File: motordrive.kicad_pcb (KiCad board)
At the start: 2 copper layers, 160 x 111.4 mm, 32 parts, among them K1 CONN_3, M1 ARDUINO, P2 CONN_25, U1 5VSWREG, U2 74HC595, U3 74HC595, U4 LM2903, U5 ULN2803, U6 ULN2803

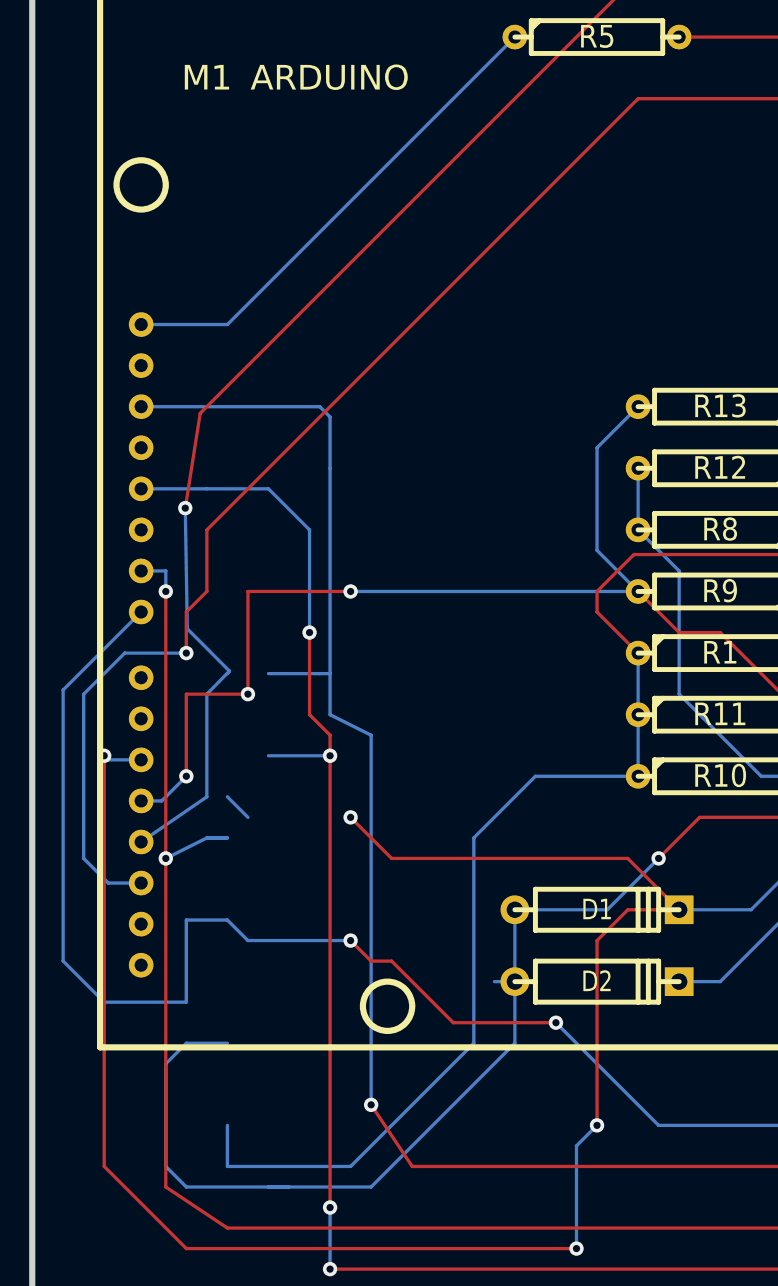
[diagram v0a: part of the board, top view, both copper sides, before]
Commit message: Tidied .brd and saved, no other changes
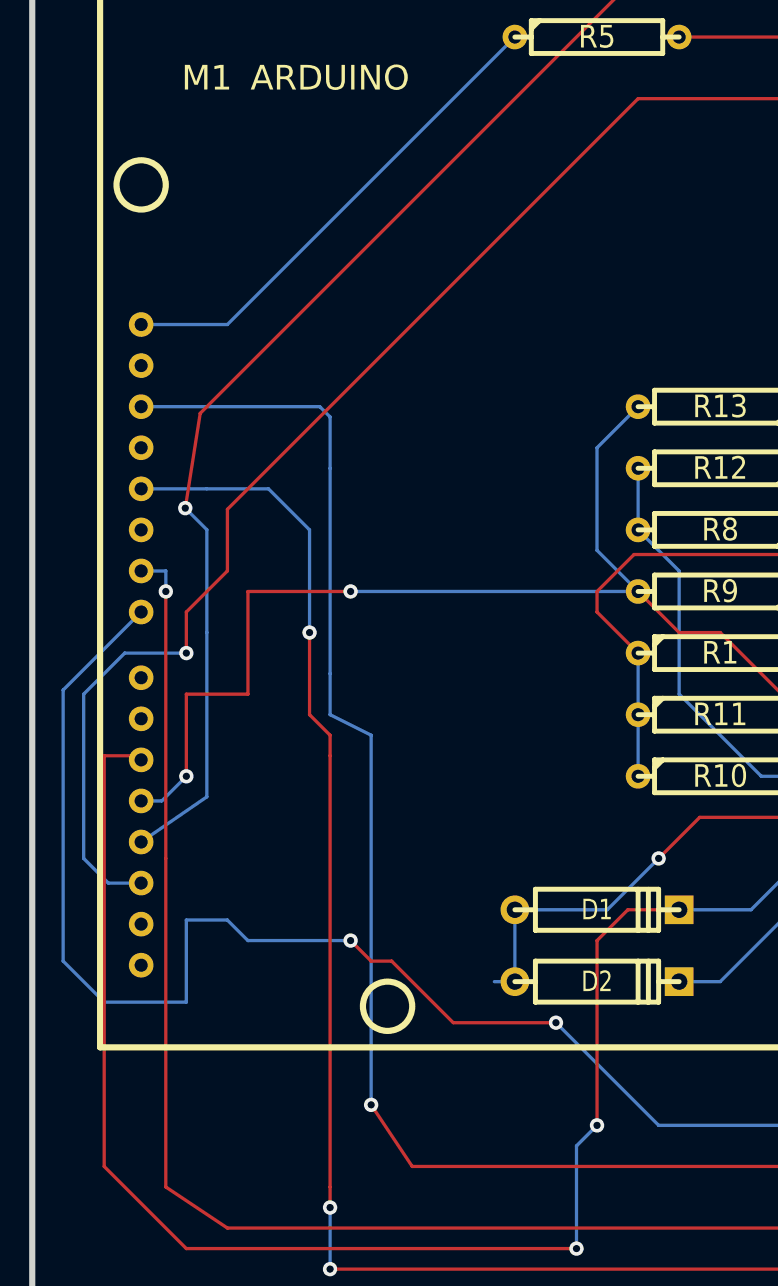
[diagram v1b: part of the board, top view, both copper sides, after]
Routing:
- net +5V: track 253.0 -> 207.6 mm
- net GND: track 302.6 -> 261.0 mm
- net N-0000037: track 147.8 -> 123.3 mm, vias 4 -> 2
- net N-0000018: track 167.7 -> 162.3 mm, vias 3 -> 2
- net N-0000049: track 150.6 -> 146.8 mm, vias 4 -> 3
- net N-0000023: track 184.2 -> 180.4 mm
- net N-000004: track 166.7 -> 165.4 mm
- net N-0000047: vias 4 -> 3

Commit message: Actually commit all - new ratsnest too
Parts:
- removed M1: ARDUINO, Arduino_rev
- removed R1: n/f, R4
- removed U2, U3: 74HC595, DIP-16__300
- added J1: TI_CONN_LAUNCHPAD, Conn_Launch_Pad, F.Cu at (21.6, 127.0)
- moved R5 86.0 mm to (158.8, 76.2)
- moved D2 66.7 mm to (99.1, 53.3), turned to 180 degrees
- moved D1 60.3 mm to (99.1, 55.9), turned to 180 degrees
- moved R10 54.7 mm to (86.4, 48.3)
- moved R11 48.4 mm to (86.4, 50.8)
- moved R9 43.9 mm to (99.1, 50.8)
- moved R8 42.7 mm to (99.1, 48.3)
- moved R12 41.5 mm to (99.1, 45.7)
- moved R13 40.4 mm to (99.1, 43.2)
- moved C2 37.7 mm to (163.8, 97.8)
- moved F1 23.4 mm to (130.8, 55.9), turned to 180 degrees
- moved C1 18.9 mm to (167.6, 97.8)
- moved U6 18.1 mm to (146.1, 62.2), turned to 0 degrees
- moved U5 17.4 mm to (119.4, 62.2), turned to 0 degrees
- moved R7 14.1 mm to (175.3, 82.5), turned to 0 degrees
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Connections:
- R5 pad 1: N-0000024 (its old number) -> (no net)
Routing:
- net GND: track 261.0 -> 45.1 mm, vias 5 -> 2
- net +5V: track 207.6 -> 0.00 mm, vias 2 -> 0
- net N-0000078: track 195.3 -> 0.00 mm, vias 3 -> 0
- net N-0000023: track 180.4 -> 0.00 mm, vias 3 -> 0
- net N-0000034 (its old number): track 174.7 -> 0.00 mm, vias 4 -> 0
- net N-0000030: track 165.4 -> 0.00 mm, vias 2 -> 0
- net N-0000018: track 162.3 -> 0.00 mm, vias 2 -> 0
- net N-0000049 (its old number): track 146.8 -> 0.00 mm, vias 3 -> 0
- net N-00000102: track 123.3 -> 0.00 mm, vias 2 -> 0
- net N-0000031: track 104.7 -> 0.00 mm, vias 1 -> 0
- net +24V: track 165.4 -> 63.8 mm, vias 2 -> 0
- net /640mV: track 97.7 -> 0.00 mm
- net N-0000015: track 95.7 -> 0.00 mm
- net N-0000044: track 92.9 -> 0.00 mm, vias 3 -> 0
- net N-0000096: track 79.4 -> 0.00 mm
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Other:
- board size 160 x 111.4 mm -> 286.4 x 163.2 mm

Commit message: Some routing
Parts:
- moved R12 94.5 mm to (43.2, 121.9), turned to 0 degrees
- moved R10 85.2 mm to (57.1, 128.3), turned to 180 degrees
- moved R8 84.7 mm to (57.1, 121.9)
- moved D1 80.4 mm to (57.1, 124.5)
- moved R13 80.0 mm to (85.1, 121.9)
- moved R11 79.0 mm to (71.1, 128.3)
- moved R9 76.4 mm to (71.1, 121.9), turned to 0 degrees
- moved D2 76.4 mm to (71.1, 124.5), turned to 0 degrees
- moved F1 33.0 mm to (97.8, 57.1), turned to 90 degrees
- moved U5 7.73 mm to (111.8, 63.5)
- moved U6 2.84 mm to (143.5, 63.5)
- moved C3 1.27 mm to (174.0, 86.4)
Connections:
- D2 pad 2: N-0000044 (its old number) -> N-0000057
- J1 pad 39: (no net) -> N-0000056
- J1 pad 40: (no net) -> N-0000029
- J1 pad 48: (no net) -> N-0000057
- J1 pad 57: N-0000044 (its old number) -> (no net)
- R11 pad 2: N-0000044 (its old number) -> N-0000057
- R13 pad 2: N-0000044 (its old number) -> N-0000057
- R2 pad 2: N-0000078 -> N-0000056
- R3 pad 2: N-0000030 -> N-0000029
- R5 pad 1: (no net) -> +5V
- R9 pad 2: N-0000044 (its old number) -> N-0000057
- U4 pad 1: N-0000030 -> N-0000029
- U4 pad 7: N-0000078 -> N-0000056
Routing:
- net N-0000097: track 0.00 -> 162.4 mm
- net GNDA: track 107.8 -> 8.23 mm, vias 1 -> 0
- net N-0000042: track 63.6 -> 0.00 mm
- net N-00000105: track 0.00 -> 50.4 mm
- net N-0000098: track 0.00 -> 45.3 mm
- net GND: track 45.1 -> 0.00 mm, vias 2 -> 1
- net N-000009: track 0.00 -> 38.3 mm
- net N-00000101: track 33.0 -> 0.00 mm
- net N-0000099: track 0.00 -> 29.9 mm
- net N-0000024: track 0.00 -> 15.1 mm
- net N-0000093: track 0.00 -> 14.6 mm
- net N-0000040: track 0.00 -> 13.5 mm
- net N-0000010: track 0.00 -> 13.3 mm
- net N-00000102: track 0.00 -> 13.0 mm
- net N-00000108: track 0.00 -> 6.67 mm
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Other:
- board size 286.4 x 163.2 mm -> 160.7 x 100.3 mm

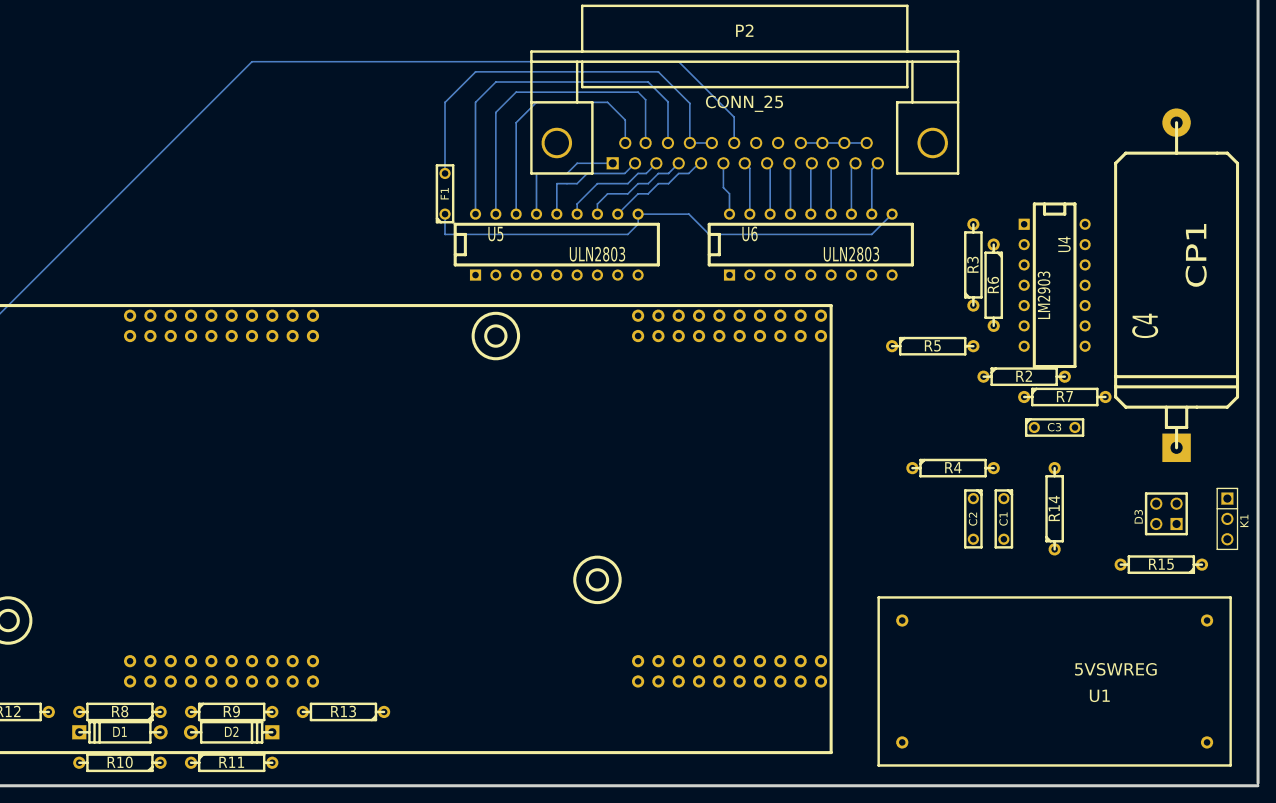
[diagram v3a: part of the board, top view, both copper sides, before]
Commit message: Finished Initial routing og PCB
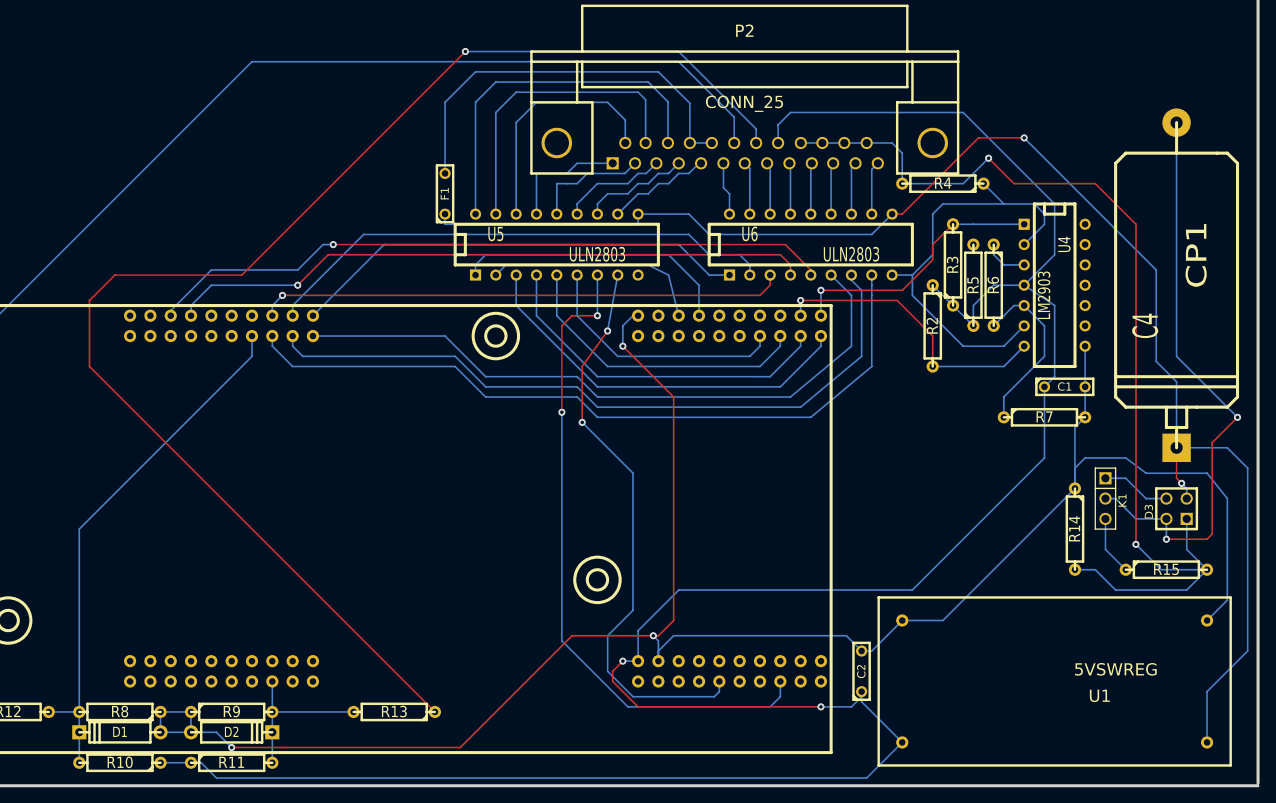
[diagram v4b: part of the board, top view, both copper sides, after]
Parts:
- removed C3: C, C2
- moved R4 35.6 mm to (160.0, 55.9), turned to 180 degrees
- moved C2 23.6 mm to (149.9, 116.8), turned to 90 degrees
- moved C1 18.2 mm to (175.3, 81.3), turned to 0 degrees
- moved K1 15.5 mm to (180.3, 95.2)
- moved R2 13.1 mm to (158.8, 73.7), turned to 270 degrees
- moved R5 9.16 mm to (163.8, 68.6), turned to 90 degrees
- moved R13 6.35 mm to (91.4, 121.9)
- moved R14 3.59 mm to (176.5, 99.1), turned to 270 degrees
- moved R7 3.59 mm to (172.7, 85.1)
- moved R3 2.54 mm to (161.3, 66.0)
- moved D3 1.42 mm to (189.2, 96.5)
- moved R15 0.90 mm to (188.0, 104.1), turned to 0 degrees
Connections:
- J1 pad 11: N-0000025 (its old number) -> +5V
- U1 pad 3: N-0000025 (its old number) -> +5V
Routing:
- net +5V: track 0.00 -> 301.1 mm, vias 0 -> 2
- net GND: track 0.00 -> 247.9 mm, vias 1 -> 3
- net N-000005: track 0.00 -> 171.3 mm, vias 0 -> 1
- net GNDA: track 8.23 -> 127.2 mm, vias 0 -> 2
- net +24V: track 62.3 -> 180.8 mm, vias 0 -> 2
- net N-0000036: track 0.00 -> 93.6 mm
- net N-0000037: track 0.00 -> 88.5 mm
- net N-0000024: track 0.00 -> 86.0 mm, vias 0 -> 1
- net N-0000023: track 0.00 -> 82.7 mm
- net N-0000044: track 0.00 -> 82.6 mm, vias 0 -> 2
- net N-0000025: track 0.00 -> 80.6 mm, vias 0 -> 1
- net N-0000042: track 0.00 -> 73.1 mm, vias 0 -> 2
- net N-0000045: track 0.00 -> 71.4 mm, vias 0 -> 2
- net N-0000043: track 0.00 -> 66.1 mm
- net N-0000026: track 0.00 -> 65.8 mm, vias 0 -> 1
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
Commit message: new updates
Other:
- board size 160.7 x 100.3 mm -> 181 x 100.3 mm
- net class FatTrack added: clearance 0.254, trace_width 0.8, via_dia 0.889, via_drill 0.635

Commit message: test add
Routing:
- net N-000005: track 171.3 -> 172.4 mm
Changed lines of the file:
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@@
   )
   (setup
-    (last_trace_width 0.2032)
+    (last_trace_width 0.5)
+    (user_trace_width 0.5)
+    (user_trace_width 0.8)
+    (user_trace_width 1)
+    (user_trace_width 1.5)
+    (user_trace_width 2)
     (trace_clearance 0.254)
     (zone_clearance 0.508)
@@
   (segment (start 69.215 130.175) (end 150.495 130.175) (width 0.2032) (layer Back) (net 2))
   (segment (start 67.31 128.27) (end 69.215 130.175) (width 0.2032) (layer Back) (net 2))
-  (segment (start 62.23 128.27) (end 66.04 128.27) (width 0.2032) (layer Back) (net 2))
+  (segment (start 62.23 128.27) (end 66.04 128.27) (width 0.8) (layer Back) (net 2))
   (segment (start 121.92 115.57) (end 120.015 115.57) (width 0.2032) (layer Back) (net 2))
   (segment (start 149.86 120.015) (end 149.86 119.38) (width 0.2032) (layer Back) (net 2))
@@
   (via (at 71.12 126.365) (size 0.889) (layers Front Back) (net 5))
   (segment (start 69.215 124.46) (end 71.12 126.365) (width 0.2032) (layer Back) (net 5))
-  (segment (start 62.23 121.92) (end 66.04 121.92) (width 0.2032) (layer Back) (net 5))
-  (segment (start 62.23 124.46) (end 62.23 121.92) (width 0.2032) (layer Back) (net 5))
-  (segment (start 66.04 124.46) (end 62.23 124.46) (width 0.2032) (layer Back) (net 5))
-  (segment (start 66.04 121.92) (end 66.04 124.46) (width 0.2032) (layer Back) (net 5))
+  (segment (start 62.23 121.92) (end 66.04 121.92) (width 0.8) (layer Back) (net 5))
+  (segment (start 62.23 124.46) (end 62.23 121.92) (width 0.8) (layer Back) (net 5))
+  (segment (start 66.04 124.46) (end 62.23 124.46) (width 0.8) (layer Back) (net 5))
+  (segment (start 66.04 121.92) (end 66.04 124.46) (width 0.8) (layer Back) (net 5))
   (segment (start 124.46 115.57) (end 124.46 114.3) (width 0.2032) (layer Back) (net 5))
   (segment (start 124.46 114.3) (end 126.365 112.395) (width 0.2032) (layer Back) (net 5))
@@
   (segment (start 132.588 56.388) (end 132.588 53.34) (width 0.2032) (layer Back) (net 35))
   (segment (start 133.35 57.15) (end 132.588 56.388) (width 0.2032) (layer Back) (net 35))
-  (segment (start 38.1 121.92) (end 38.1 76.2) (width 0.2032) (layer Back) (net 36))
-  (segment (start 133.9342 47.5742) (end 133.9342 50.8) (width 0.2032) (layer Back) (net 36))
-  (segment (start 127 40.64) (end 133.9342 47.5742) (width 0.2032) (layer Back) (net 36))
-  (segment (start 73.66 40.64) (end 127 40.64) (width 0.2032) (layer Back) (net 36))
-  (segment (start 38.1 76.2) (end 73.66 40.64) (width 0.2032) (layer Back) (net 36))
+  (segment (start 38.1 121.92) (end 38.1 76.2) (width 0.8) (layer Back) (net 36))
+  (segment (start 38.1 76.2) (end 73.66 40.64) (width 0.8) (layer Back) (net 36))
+  (segment (start 73.66 40.64) (end 127 40.64) (width 0.8) (layer Back) (net 36))
+  (segment (start 127 40.64) (end 133.9342 47.5742) (width 0.8) (layer Back) (net 36))
+  (segment (start 133.9342 47.5742) (end 133.9342 50.8) (width 0.8) (layer Back) (net 36))
   (segment (start 116.84 59.69) (end 116.84 58.42) (width 0.2032) (layer Back) (net 37))
   (segment (start 125.73 54.61) (end 127 53.34) (width 0.2032) (layer Back) (net 37))
@@
   (segment (start 118.11 57.15) (end 120.65 57.15) (width 0.2032) (layer Back) (net 37))
   (segment (start 116.84 58.42) (end 118.11 57.15) (width 0.2032) (layer Back) (net 37))
-  (segment (start 76.2 121.92) (end 86.36 121.92) (width 0.2032) (layer Back) (net 38))
-  (segment (start 76.2 124.46) (end 76.2 121.92) (width 0.2032) (layer Back) (net 38))
-  (segment (start 76.2 128.27) (end 76.2 124.46) (width 0.2032) (layer Back) (net 38))
-  (segment (start 76.2 121.92) (end 76.2 118.11) (width 0.2032) (layer Back) (net 38))
+  (segment (start 76.2 121.92) (end 86.36 121.92) (width 0.8) (layer Back) (net 38))
+  (segment (start 76.2 124.46) (end 76.2 121.92) (width 0.8) (layer Back) (net 38))
+  (segment (start 76.2 128.27) (end 76.2 124.46) (width 0.8) (layer Back) (net 38))
+  (segment (start 76.2 121.92) (end 76.2 118.11) (width 0.8) (layer Back) (net 38))
   (segment (start 189.23 48.26) (end 189.23 77.47) (width 0.2032) (layer Back) (net 39))
   (segment (start 187.96 100.33) (end 187.96 97.79) (width 0.2032) (layer Back) (net 39))
@@
   (segment (start 73.66 77.47) (end 73.66 74.93) (width 0.2032) (layer Back) (net 40))
   (segment (start 52.07 99.06) (end 73.66 77.47) (width 0.2032) (layer Back) (net 40))
-  (segment (start 52.07 124.46) (end 52.07 128.27) (width 0.2032) (layer Back) (net 40))
-  (segment (start 52.07 121.92) (end 52.07 124.46) (width 0.2032) (layer Back) (net 40))
-  (segment (start 48.26 121.92) (end 52.07 121.92) (width 0.2032) (layer Back) (net 40))
+  (segment (start 52.07 124.46) (end 52.07 128.27) (width 0.8) (layer Back) (net 40))
+  (segment (start 52.07 121.92) (end 52.07 124.46) (width 0.8) (layer Back) (net 40))
+  (segment (start 48.26 121.92) (end 52.07 121.92) (width 0.8) (layer Back) (net 40))
   (segment (start 139.7 118.11) (end 139.7 120.015) (width 0.2032) (layer Back) (net 41))
   (segment (start 116.84 72.39) (end 116.84 67.31) (width 0.2032) (layer Back) (net 41))
@@
   (segment (start 143.51 59.69) (end 143.51 53.467) (width 0.2032) (layer Back) (net 44))
   (segment (start 143.51 53.467) (end 143.637 53.34) (width 0.2032) (layer Back) (net 44))
-  (segment (start 136.6774 50.8) (end 136.6774 49.0474) (width 0.2032) (layer Back) (net 45))
-  (segment (start 53.34 78.74) (end 96.52 121.92) (width 0.2032) (layer Front) (net 45))
-  (segment (start 53.34 70.485) (end 53.34 78.74) (width 0.2032) (layer Front) (net 45))
-  (segment (start 56.515 67.31) (end 53.34 70.485) (width 0.2032) (layer Front) (net 45))
-  (segment (start 72.39 67.31) (end 56.515 67.31) (width 0.2032) (layer Front) (net 45))
-  (segment (start 100.33 39.37) (end 72.39 67.31) (width 0.2032) (layer Front) (net 45))
-  (via (at 100.33 39.37) (size 0.889) (layers Front Back) (net 45))
-  (segment (start 127 39.37) (end 100.33 39.37) (width 0.2032) (layer Back) (net 45))
-  (segment (start 136.6774 49.0474) (end 127 39.37) (width 0.2032) (layer Back) (net 45))
+  (segment (start 136.6774 50.8) (end 136.6774 48.4124) (width 0.5) (layer Back) (net 45) (status 400000))
+  (segment (start 53.34 78.74) (end 96.52 121.92) (width 0.5) (layer Front) (net 45))
+  (segment (start 53.34 70.485) (end 53.34 78.74) (width 0.5) (layer Front) (net 45))
+  (segment (start 56.515 67.31) (end 53.34 70.485) (width 0.5) (layer Front) (net 45))
+  (segment (start 72.39 67.31) (end 56.515 67.31) (width 0.5) (layer Front) (net 45))
+  (segment (start 100.33 38.735) (end 72.39 67.31) (width 0.5) (layer Front) (net 45))
+  (via (at 100.33 38.735) (size 0.889) (layers Front Back) (net 45))
+  (segment (start 127 38.735) (end 100.33 38.735) (width 0.5) (layer Back) (net 45))
+  (segment (start 136.6774 48.4124) (end 127 38.735) (width 0.5) (layer Back) (net 45))
   (segment (start 180.34 97.79) (end 180.34 101.6) (width 0.2032) (layer Back) (net 46))
   (segment (start 180.34 101.6) (end 182.88 104.14) (width 0.2032) (layer Back) (net 46))

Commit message: decent track widths
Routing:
- net N-0000025: track 80.6 -> 128.2 mm, vias 1 -> 3
- net N-000002: track 54.9 -> 95.8 mm
- net N-0000044: track 82.6 -> 93.7 mm
- net N-0000030: track 49.5 -> 58.9 mm
- net N-0000036: track 93.6 -> 102.4 mm
- net N-0000037: track 88.5 -> 94.8 mm
- net N-0000034: track 33.1 -> 38.7 mm
- net N-0000023: track 82.7 -> 87.5 mm
- net N-0000024: track 86.0 -> 89.5 mm, vias 1 -> 0
- net N-0000017: track 13.0 -> 15.8 mm
- net /640mV: track 5.61 -> 8.15 mm
- net N-0000045: track 71.4 -> 73.8 mm
- net N-0000033: track 36.5 -> 34.3 mm, vias 1 -> 0
- net GND: track 247.9 -> 245.8 mm
- net +5V: track 301.1 -> 302.3 mm
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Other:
- board outline removed
- net class FatTrack removed

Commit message: bit of shuffling
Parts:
- moved R12 78.8 mm to (88.9, 57.8), turned to 180 degrees
- moved R10 77.3 mm to (76.2, 53.3), turned to 0 degrees
- moved R11 75.4 mm to (62.9, 53.3), turned to 180 degrees
- moved R13 75.3 mm to (68.6, 50.2)
- moved D1 70.6 mm to (76.2, 56.5), turned to 0 degrees
- moved D2 68.4 mm to (62.9, 56.5), turned to 180 degrees
- moved R8 64.7 mm to (76.8, 60.3), turned to 0 degrees
- moved R9 61.5 mm to (62.9, 61.0), turned to 180 degrees
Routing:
- net N-000004: track 161.6 -> 53.1 mm
- net N-000005: track 171.3 -> 72.7 mm, vias 1 -> 0
- net N-0000041: track 20.3 -> 105.7 mm
- net GND: track 245.8 -> 259.6 mm, vias 3 -> 5
- net +5V: track 302.3 -> 291.7 mm
- net N-0000020: track 50.4 -> 42.9 mm
- net N-0000010: track 45.3 -> 39.2 mm
- net N-0000043: track 66.1 -> 71.6 mm
- net N-0000014: track 38.3 -> 33.7 mm
- net N-000009: track 29.9 -> 28.3 mm
